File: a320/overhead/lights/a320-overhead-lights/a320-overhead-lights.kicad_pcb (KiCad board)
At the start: 2 copper layers, 77.5 x 107.5 mm, 29 parts, among them J1 Conn_02x11_Odd_Even, J10 Conn_02x08_Odd_Even, J11 Conn_02x08_Odd_Even, J12 Conn_02x08_Odd_Even, J13 Conn_02x08_Odd_Even, J14 Conn_02x08_Odd_Even, J15 Conn_02x08_Odd_Even, J2 Conn_02x08_Odd_Even, J3 Conn_02x03_Odd_Even, J4 Conn_02x08_Odd_Even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

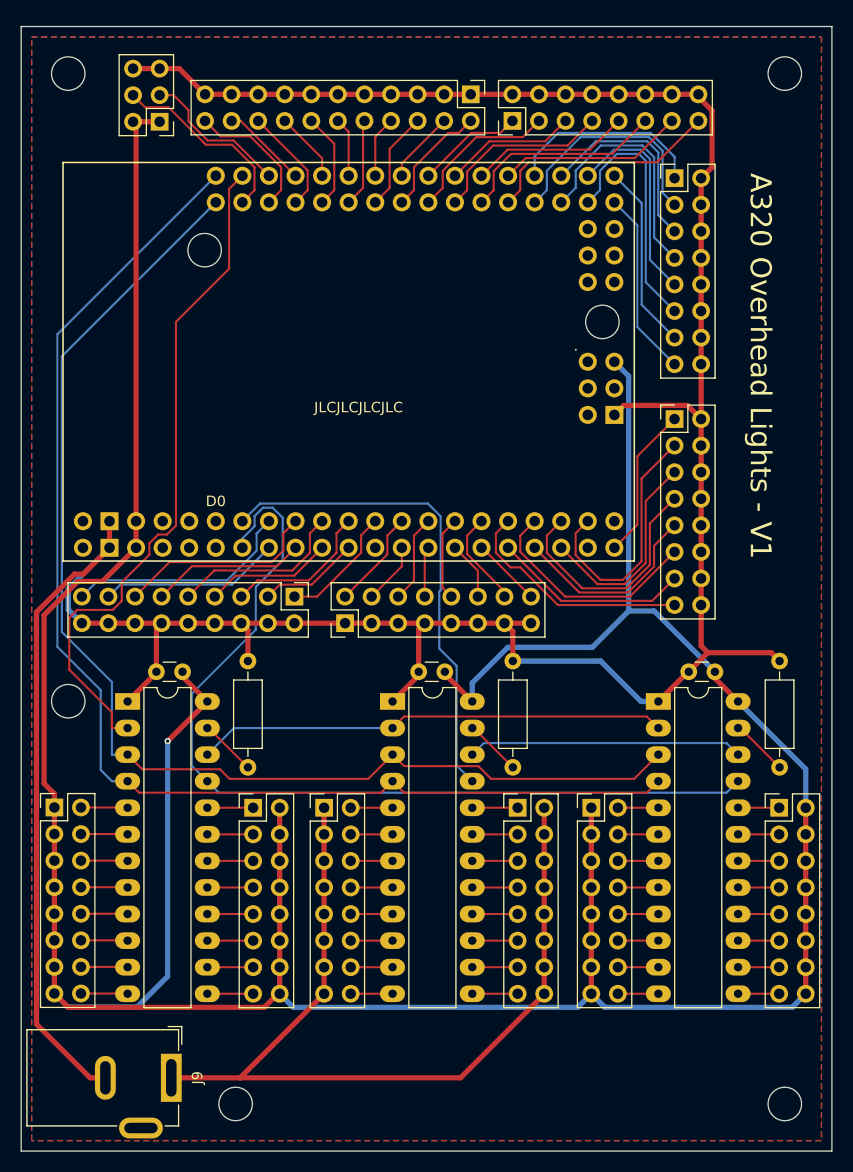
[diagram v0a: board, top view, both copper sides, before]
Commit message: a320 overhead lights - added labels to pcb
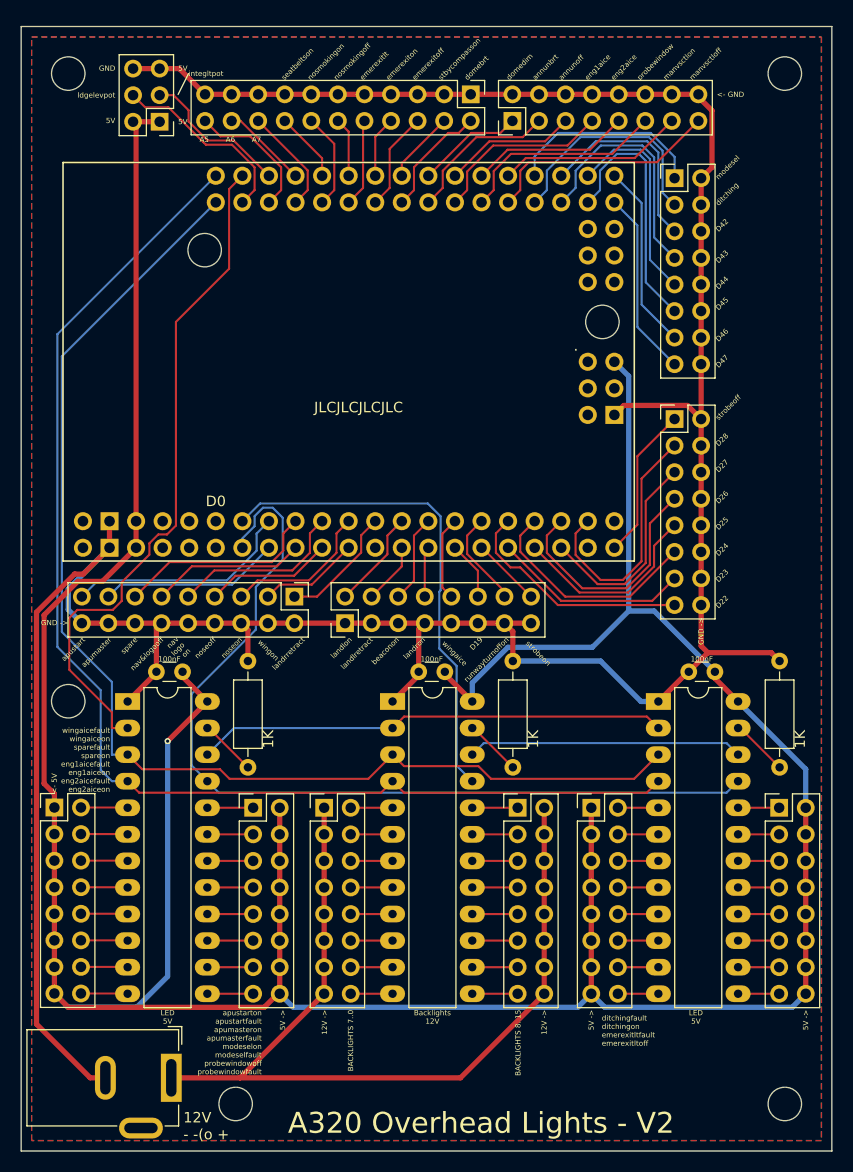
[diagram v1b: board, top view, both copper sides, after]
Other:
- board text added: "100nF"
- board text added: "12V - -(o +"
- board text added: "12V ->"
- board text added: "1K"
- board text added: "5V"
- board text added: "5V ->"
- board text added: "<- 5V"
- board text added: "<- GND"
- board text added: "A320 Overhead Lights - V2"
- board text added: "A5"
- board text added: "A6"
- board text added: "A7"
- board text added: "BACKLIGHTS 7..0"
- board text added: "BACKLIGHTS 8..15"
- board text added: "Backlights 12V"
- board text added: "D19"
- board text added: "D22"
- board text added: "D23"
- board text added: "D24"
- board text added: "D25"
- board text added: "D26"
- board text added: "D27"
- board text added: "D28"
- board text added: "D42"
- board text added: "D43"
- board text added: "D44"
- board text added: "D45"
- board text added: "D46"
- board text added: "D47"
- board text added: "GND"
- board text added: "GND ->"
- board text added: "LED 5V"
- board text added: "annunbrt"
- board text added: "annunoff"
- board text added: "apumaster"
- board text added: "apustart"
- board text added: "apustarton apustartfault apumasteron apumasterfault modeselon modeselfault probewindowoff probewindowfault"
- board text added: "beaconon"
- board text added: "ditching"
- board text added: "ditchingfault ditchingon emerexitltfault emerexitltoff"
- board text added: "domebrt"
- board text added: "domedim"
- board text added: "emerexitlt"
- board text added: "emerexitoff"
- board text added: "emerexiton"
- board text added: "eng1aice"
- board text added: "eng2aice"
- board text added: "integltpot"
- board text added: "landlon"
- board text added: "landlretract"
- board text added: "landron"
- board text added: "landrretract"
- board text added: "ldgelevpot"
- board text added: "manvsctloff"
- board text added: "manvsctlon"
- board text added: "modesel"
- board text added: "nav logo on"
- board text added: "nav&logooff"
- board text added: "noseoff"
- board text added: "noseon"
- board text added: "nosmokingoff"
- board text added: "nosmokingon"
- board text added: "probewindow"
- board text added: "runwayturnoffon"
- board text added: "seatbeltson"
- board text added: "spare"
- board text added: "stbycompasson"
- board text added: "strobeoff"
- board text added: "strobeon"
- board text added: "wingaice"
- board text added: "wingaicefault wingaiceon sparefault spareon eng1aicefault eng1aiceon eng2aicefault eng2aiceon"
- board text added: "wingon"
- board text removed: "A320 Overhead Lights - V1"

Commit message: a320 overhead lights - moved led drivers around and re-routed
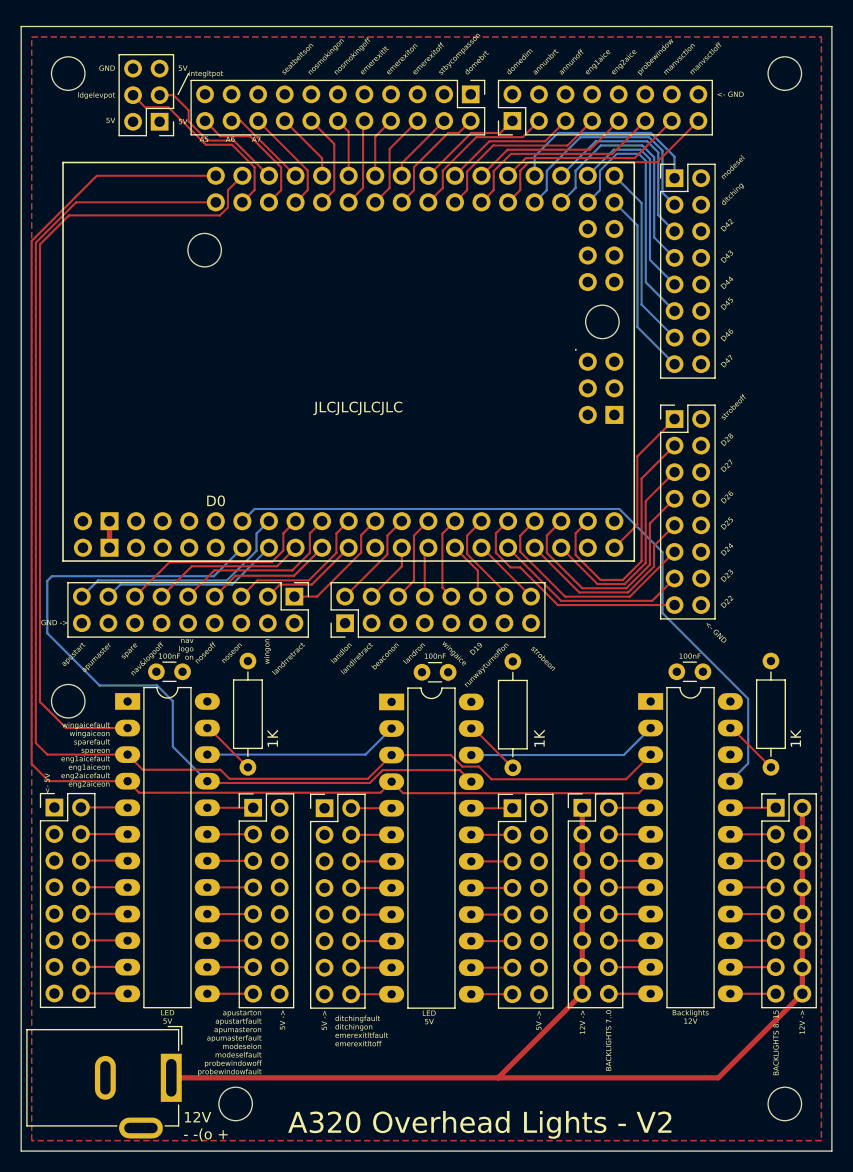
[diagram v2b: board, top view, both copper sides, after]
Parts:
- moved C3 25.5 mm to (140.8, 111.7)
- moved J14 25.5 mm to (147.0, 124.7)
- moved J15 25.5 mm to (129.0, 124.7)
- moved R3 25.5 mm to (147.0, 110.7)
- moved U3 25.5 mm to (135.4, 114.6)
- moved C2 24.7 mm to (165.2, 111.7)
- moved R2 24.7 mm to (171.7, 110.7)
- moved U2 24.7 mm to (160.2, 114.5)
- moved J11 24.7 mm to (172.1, 124.7)
- moved J13 24.7 mm to (153.6, 124.7)
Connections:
- U2 pad 2: LEDDRV_DATA_2 -> LEDDRV_DATA_3
- U2 pad 22: LEDDRV_DATA_3 -> unconnected-(U2-SDO-Pad22)
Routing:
- net +5V: track 338.5 -> 1.31 mm, vias 1 -> 0
- net GND: track 286.2 -> 3.74 mm
- net LEDDRV_DATA_2: track 45.1 -> 18.6 mm
- net +12V: track 85.9 -> 110.6 mm
- net BACKLIGHT_BRT: track 46.8 -> 68.3 mm
- net ANNUNCIATOR_BRT: track 88.0 -> 74.9 mm
- net LEDDRV_CLK: track 116.9 -> 129.7 mm
- net LEDDRV_LATCH: track 120.4 -> 131.9 mm
- net LEDDRV_DATA: track 65.3 -> 76.2 mm
- net LEDDRV_DATA_3: track 26.3 -> 18.2 mm

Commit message: Ordered a320 overhead panel
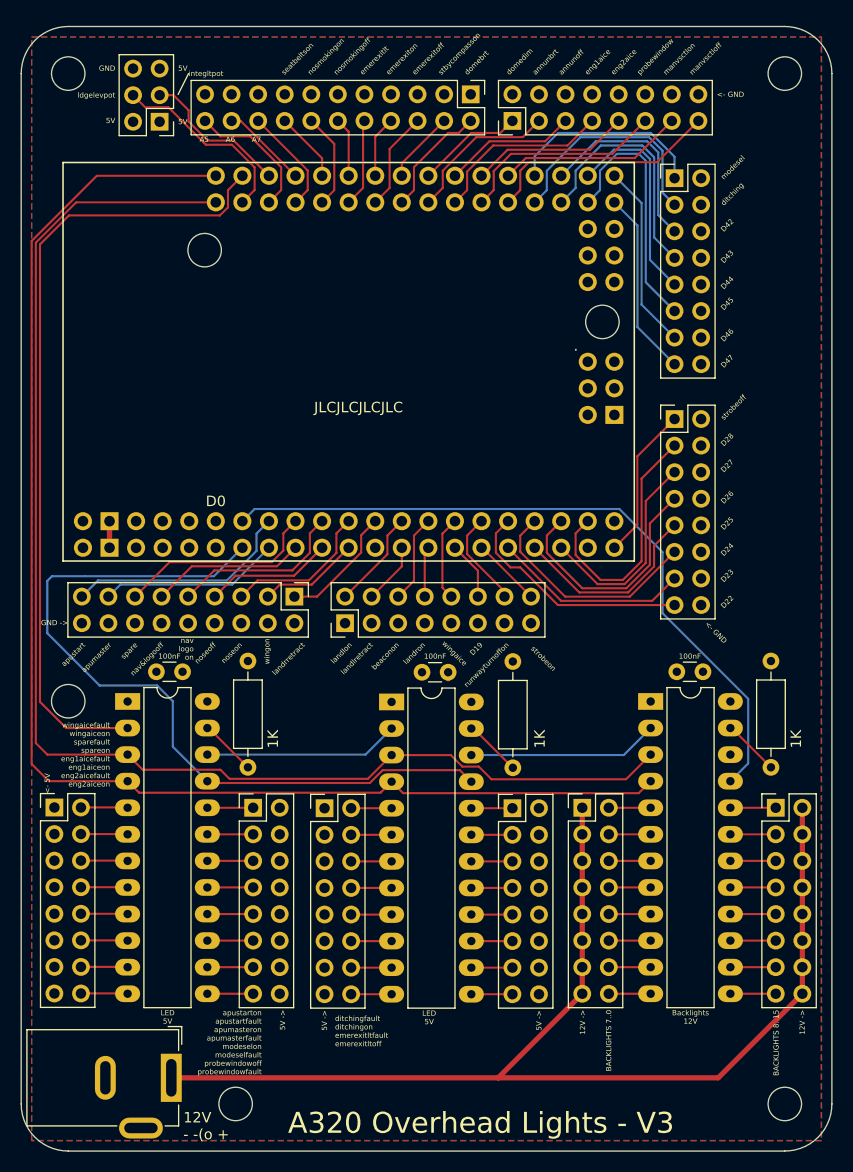
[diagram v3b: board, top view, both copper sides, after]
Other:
- outline, holes or cut-outs redrawn
- board text added: "A320 Overhead Lights - V3"
- board text removed: "A320 Overhead Lights - V2"
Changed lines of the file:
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@@
 		(layer "F.SilkS")
 	)
-	(gr_rect
-		(start 100 50)
-		(end 177.5 157.5)
+	(gr_arc
+		(start 177.5 153)
+		(mid 176.181981 156.181981)
+		(end 173 157.5)
 		(stroke
 			(width 0.05)
 			(type default)
 		)
-		(fill none)
 		(layer "Edge.Cuts")
 	)
-	(gr_text "A320 Overhead Lights - V2"
+	(gr_line
+		(start 104.5 157.5)
+		(end 173 157.5)
+		(stroke
+			(width 0.05)
+			(type default)
+		)
+		(layer "Edge.Cuts")
+	)
+	(gr_line
+		(start 100 54.5)
+		(end 100 153)
+		(stroke
+			(width 0.05)
+			(type default)
+		)
+		(layer "Edge.Cuts")
+	)
+	(gr_arc
+		(start 173 50)
+		(mid 176.181981 51.318019)
+		(end 177.5 54.5)
+		(stroke
+			(width 0.05)
+			(type default)
+		)
+		(layer "Edge.Cuts")
+	)
+	(gr_line
+		(start 173 50)
+		(end 104.5 50)
+		(stroke
+			(width 0.05)
+			(type default)
+		)
+		(layer "Edge.Cuts")
+	)
+	(gr_line
+		(start 177.5 153)
+		(end 177.5 54.5)
+		(stroke
+			(width 0.05)
+			(type default)
+		)
+		(layer "Edge.Cuts")
+	)
+	(gr_arc
+		(start 104.5 157.5)
+		(mid 101.318019 156.181981)
+		(end 100 153)
+		(stroke
+			(width 0.05)
+			(type default)
+		)
+		(layer "Edge.Cuts")
+	)
+	(gr_arc
+		(start 100 54.5)
+		(mid 101.318019 51.318019)
+		(end 104.5 50)
+		(stroke
+			(width 0.05)
+			(type default)
+		)
+		(layer "Edge.Cuts")
+	)
+	(gr_text "A320 Overhead Lights - V3"
 		(at 125.5 156 0)
 		(layer "F.SilkS")
